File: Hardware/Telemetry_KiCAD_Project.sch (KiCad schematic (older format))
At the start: 3 parts, among them J1 TX SPI Debug, J2 RX SPI Debug, J3 50Ω SMA Connector

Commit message: Routed TX Chip SPI bus
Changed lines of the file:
@@
 Wire Wire Line
 	4750 4600 4100 4600
-$Sheet
-S 2850 2100 1250 2650
-U 61A107A5
-F0 "MCU_L562VE" 50
-F1 "COMPONENT_SHEETS/MCU_L562VE.sch" 50
-F2 "I2C1_SCL" I L 2850 2550 50
-F3 "I2C1_SDA" I L 2850 2400 50
-F4 "I2C1_EN" I L 2850 2250 50
-F5 "DEBUG_SWCLK" I L 2850 4100 50
-F6 "~SPI2_NSS" I R 4100 4150 50
-F7 "SPI3_MOSI" I R 4100 2400 50
-F8 "SPI3_MISO" I R 4100 2550 50
-F9 "SPI3_SCK" I R 4100 2700 50
-F10 "DEBUG_SWDIO" I L 2850 3950 50
-F11 "USB_DP" I R 4100 4450 50
-F12 "USB_DM" I R 4100 4600 50
-F13 "SPI2_SCK" I R 4100 3850 50
-F14 "SPI2_MISO" I R 4100 3700 50
-F15 "SPI2_MOSI" I R 4100 3550 50
-F16 "~SPI3_NSS" I R 4100 3000 50
-F17 "SPI1_SCK" I L 2850 3150 50
-F18 "SPI1_MISO" I L 2850 3000 50
-F19 "SPI1_MOSI" I L 2850 2850 50
-F20 "~SPI1_NSS" I L 2850 3300 50
-F21 "NRST" I L 2850 4250 50
-F22 "ABORT_1" I L 2850 3450 50
-F23 "ABORT_2" I L 2850 3550 50
-F24 "SPI2_RST" I R 4100 4300 50
-F25 "SPI3_RST" I R 4100 3150 50
-F26 "SPI2_EXT_INT" I R 4100 4000 50
-F27 "SPI1_EXT_INT" I R 4100 2850 50
-$EndSheet
 Wire Wire Line
 	2850 2250 1250 2250
@@
 F12 "Fire_redundant" I R 1250 3550 50
 $EndSheet
+$Sheet
+S 2850 2100 1250 2650
+U 61A107A5
+F0 "MCU_L562VE" 50
+F1 "COMPONENT_SHEETS/MCU_L562VE.sch" 50
+F2 "I2C1_SCL" I L 2850 2550 50
+F3 "I2C1_SDA" I L 2850 2400 50
+F4 "I2C1_EN" I L 2850 2250 50
+F5 "DEBUG_SWCLK" I L 2850 4100 50
+F6 "~SPI2_NSS" I R 4100 4150 50
+F7 "SPI3_MOSI" I R 4100 2400 50
+F8 "SPI3_MISO" I R 4100 2550 50
+F9 "SPI3_SCK" I R 4100 2700 50
+F10 "DEBUG_SWDIO" I L 2850 3950 50
+F11 "USB_DP" I R 4100 4450 50
+F12 "USB_DM" I R 4100 4600 50
+F13 "SPI2_SCK" I R 4100 3850 50
+F14 "SPI2_MISO" I R 4100 3700 50
+F15 "SPI2_MOSI" I R 4100 3550 50
+F16 "~SPI3_NSS" I R 4100 3000 50
+F17 "SPI1_SCK" I L 2850 3150 50
+F18 "SPI1_MISO" I L 2850 3000 50
+F19 "SPI1_MOSI" I L 2850 2850 50
+F20 "~SPI1_NSS" I L 2850 3300 50
+F21 "NRST" I L 2850 4250 50
+F22 "ABORT_1" I L 2850 3450 50
+F23 "ABORT_2" I L 2850 3550 50
+F24 "SPI2_RST" I R 4100 4300 50
+F25 "SPI3_RST" I R 4100 3150 50
+F26 "SPI2_EXT_INT" I R 4100 4000 50
+F27 "SPI3_EXT_INT" I R 4100 2850 50
+$EndSheet
 $EndSCHEMATC

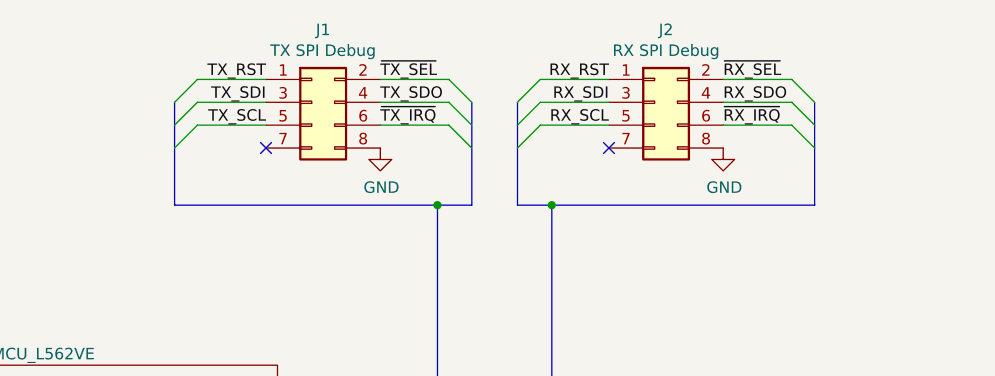
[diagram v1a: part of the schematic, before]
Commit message: Routed debug connectors
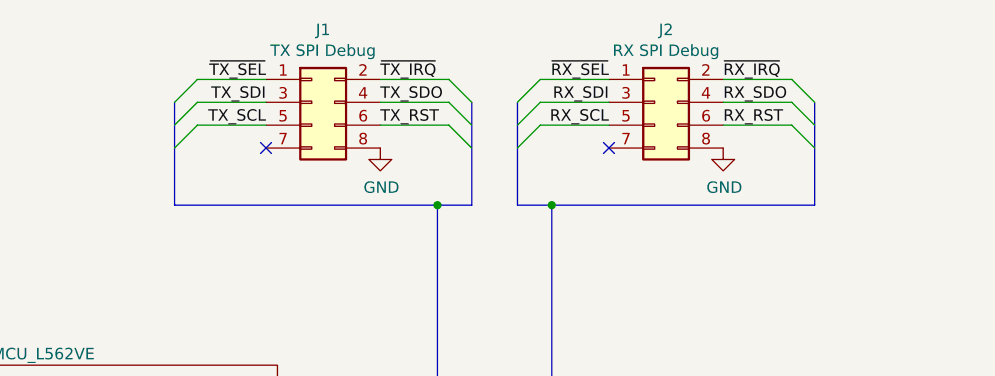
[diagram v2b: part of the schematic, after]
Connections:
- net RX_RST: now also J2.6 (Pin_6); no longer J2.1 (Pin_1)
- net TX_RST: now also J1.6 (Pin_6); no longer J1.1 (Pin_1)
- net ~RX_IRQ: now also J2.2 (Pin_2); no longer J2.6 (Pin_6)
- net ~RX_SEL: now also J2.1 (Pin_1); no longer J2.2 (Pin_2)
- net ~TX_IRQ: now also J1.2 (Pin_2); no longer J1.6 (Pin_6)
- net ~TX_SEL: now also J1.1 (Pin_1); no longer J1.2 (Pin_2)
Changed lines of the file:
@@
 	1    0    0    -1
 $EndComp
+Text Label 4050 850  2    50   ~ 0
+~TX_SEL
 Text Label 4550 850  0    50   ~ 0
-~TX_SEL
-Text Label 4550 1050 0    50   ~ 0
 ~TX_IRQ
 Text Label 4550 950  0    50   ~ 0
@@
 Text Label 4050 1050 2    50   ~ 0
 TX_SCL
+Text Label 5550 850  2    50   ~ 0
+~RX_SEL
 Text Label 6050 850  0    50   ~ 0
-~RX_SEL
-Text Label 6050 1050 0    50   ~ 0
 ~RX_IRQ
 Text Label 6050 950  0    50   ~ 0
@@
 Wire Wire Line
 	4850 1050 4550 1050
-Text Label 5550 850  2    50   ~ 0
+Text Label 6050 1050 0    50   ~ 0
 RX_RST
-Text Label 4050 850  2    50   ~ 0
+Text Label 4550 1050 0    50   ~ 0
 TX_RST
 NoConn ~ 5550 1150

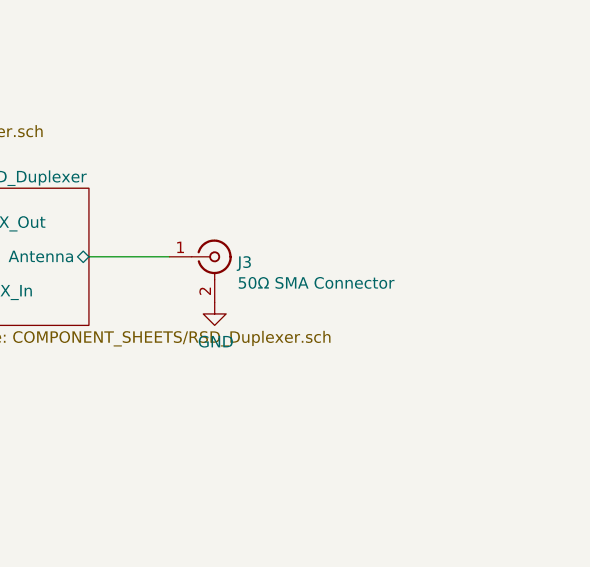
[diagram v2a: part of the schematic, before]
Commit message: Major Redesign
 - Copper ground pours on F and B.
 - Improved isolation between data lines
 - Expanded via fences around RF section.
 - GND plane isolation peninsulas for crystals.
 - Simplified I2C, SPI, and USB lines for reduced interference.
 - Added 3D models for all components.
 - Adjusted positions of RF components for improved impedance matching.
 - RF components to 0402 package from 0603 for improved impedance matching.
 - Traces for RF section have rounded corners to help improve impedance matching and reduce interference.
 - Moved silkscreen labels to outside via fence for improved legibility.
 - Improved trace thicknesses for power delivery.
 - Updated libraries to include those found in other RDT modules.
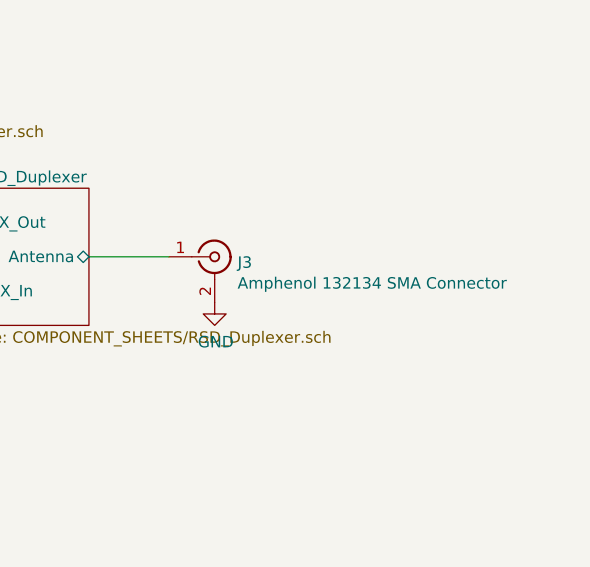
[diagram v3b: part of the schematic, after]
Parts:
- J3: value 50Ω SMA Connector -> Amphenol 132134 SMA Connector
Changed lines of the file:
@@
 P 9700 3450
 F 0 "J3" H 9800 3425 50  0000 L CNN
-F 1 "50Ω SMA Connector" H 9800 3334 50  0000 L CNN
+F 1 "Amphenol 132134 SMA Connector" H 9800 3334 50  0000 L CNN
 F 2 "Connector_Coaxial:SMA_Amphenol_132134-11_Vertical" H 9700 3450 50  0001 C CNN
-F 3 " ~" H 9700 3450 50  0001 C CNN
+F 3 "https://s3-us-west-2.amazonaws.com/catsy.582/C132134.pdf" H 9700 3450 50  0001 C CNN
 	1    9700 3450
 	1    0    0    -1
@@
 NoConn ~ 5550 1150
 NoConn ~ 4050 1150
-Wire Bus Line
-	5150 950  5150 1400
-Wire Bus Line
-	3650 950  3650 1400
-Wire Bus Line
-	6450 950  6450 1400
-Wire Bus Line
-	4950 950  4950 1400
-Wire Bus Line
-	4550 3450 4550 4200
-Wire Bus Line
-	5550 3450 5550 4300
-Wire Bus Line
-	5550 2250 5550 3000
-Wire Bus Line
-	4550 2250 4550 3050
 $Sheet
 S 750  2100 500  2250
@@
 F27 "SPI3_EXT_INT" I R 4100 2850 50
 $EndSheet
+Wire Bus Line
+	5150 950  5150 1400
+Wire Bus Line
+	3650 950  3650 1400
+Wire Bus Line
+	6450 950  6450 1400
+Wire Bus Line
+	4950 950  4950 1400
+Wire Bus Line
+	4550 3450 4550 4200
+Wire Bus Line
+	5550 3450 5550 4300
+Wire Bus Line
+	5550 2250 5550 3000
+Wire Bus Line
+	4550 2250 4550 3050
 $EndSCHEMATC
